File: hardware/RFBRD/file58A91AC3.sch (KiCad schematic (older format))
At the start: 19 parts

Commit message: Added bits of the RF Board, dumped to PCB.
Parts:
- added C34: 0.1uF, Capacitors_SMD:C_0805, symbol C
- added C35: 1uF, Capacitors_SMD:C_0805, symbol C
- added C36: 10uF, Capacitors_SMD:C_0805, symbol C
- added D1, D2: LED, LEDs:LED_0603, symbol LED
- added P1: CONN_01X08, Pin_Headers:Pin_Header_Straight_1x08, symbol CONN_01X08
- added R13: 1K, Resistors_SMD:R_0805, symbol R
- added W1, W2, W3, W4, W5, W6, W7, W8: TEST_1P, Measurement_Points:Test_Point_Keystone_5019_Minature, symbol TEST_1P
- 16MHz1: renamed from 16MHz; footprint (none) -> Crystals:Crystal_HC49-SD_SMD
- 9pF1, 9pF2: renamed from 9pF; footprint (none) -> Capacitors_SMD:C_0805
- C1, C2, C3, C4, C5, C6, C7, C8, C9: renamed from C?; footprint (none) -> Capacitors_SMD:C_0805
- L1: renamed from L?; footprint (none) -> Choke_SMD:Choke_SMD_7.3x7.3_H4.5
- L2, L3, L4, L5, L6: renamed from L?; footprint (none) -> Resistors_SMD:R_0805
- U1: renamed from U?; footprint (none) -> Housings_DFN_QFN:QFN-28-1EP_5x5mm_Pitch0.5mm
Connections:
- net labels added: VCC
- wire segments 76 -> 103
- no-connect marks 7 -> 8

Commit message: Added some Amplification Chain work.
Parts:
- removed W8: TEST_1P, Measurement_Points:Test_Point_Keystone_5019_Minature, symbol TEST_1P
- C37: renamed from 9pF1; value C -> 20pF
- C38: renamed from 9pF2; value C -> 20pF
- Y1: renamed from 16MHz1; value Crystal -> 16MHz
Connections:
- wire segments 103 -> 102
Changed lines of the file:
@@
 $EndComp
 $Comp
-L Crystal 16MHz1
+L Crystal Y1
 U 1 1 58A92FB4
 P 5550 2050
-F 0 "16MHz1" H 5550 2200 50  0000 C CNN
-F 1 "Crystal" H 5550 1900 50  0000 C CNN
+F 0 "Y1" H 5550 2200 50  0000 C CNN
+F 1 "16MHz" H 5550 1900 50  0000 C CNN
 F 2 "Crystals:Crystal_HC49-SD_SMD" H 5550 2050 50  0001 C CNN
 F 3 "" H 5550 2050 50  0000 C CNN
@@
 Connection ~ 5750 2050
 $Comp
-L C 9pF1
+L C C37
 U 1 1 58A93009
 P 5350 1700
-F 0 "9pF1" H 5375 1800 50  0000 L CNN
-F 1 "C" H 5375 1600 50  0000 L CNN
+F 0 "C37" H 5375 1800 50  0000 L CNN
+F 1 "20pF" H 5375 1600 50  0000 L CNN
 F 2 "Capacitors_SMD:C_0805" H 5388 1550 50  0001 C CNN
 F 3 "" H 5350 1700 50  0000 C CNN
@@
 $EndComp
 $Comp
-L C 9pF2
+L C C38
 U 1 1 58A93027
 P 5750 1700
-F 0 "9pF2" H 5775 1800 50  0000 L CNN
-F 1 "C" H 5775 1600 50  0000 L CNN
+F 0 "C38" H 5775 1800 50  0000 L CNN
+F 1 "20pF" H 5775 1600 50  0000 L CNN
 F 2 "Capacitors_SMD:C_0805" H 5788 1550 50  0001 C CNN
 F 3 "" H 5750 1700 50  0000 C CNN
@@
 Text GLabel 8700 1500 2    60   Input ~ 0
 uc_clk
-$Comp
-L TEST_1P W8
-U 1 1 58C35CC6
-P 9600 700
-F 0 "W8" H 9600 970 50  0000 C CNN
-F 1 "TEST_1P" H 9600 900 50  0000 C CNN
-F 2 "Measurement_Points:Test_Point_Keystone_5019_Minature" H 9800 700 50  0001 C CNN
-F 3 "" H 9800 700 50  0000 C CNN
-	1    9600 700
-	0    -1   -1   0
-$EndComp
-Wire Wire Line
-	9600 700  9700 700
-Text GLabel 9700 700  2    60   Input ~ 0
-PWRAMP_SEL
 $EndSCHEMATC

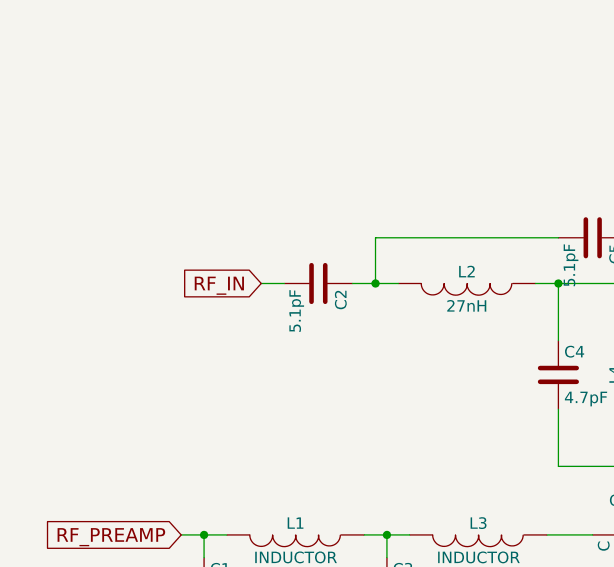
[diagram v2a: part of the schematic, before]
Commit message: Added Internals of Board.
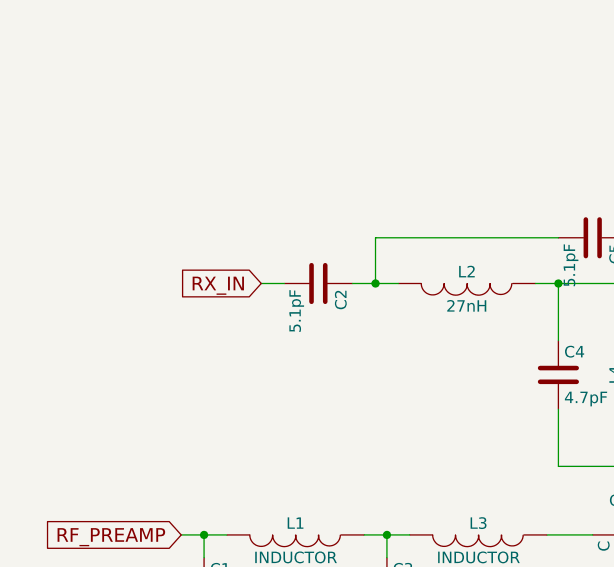
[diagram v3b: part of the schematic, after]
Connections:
- net labels added: RX_IN
- net labels removed: RF_IN
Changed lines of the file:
@@
 LIBS:contrib
 LIBS:valves
-LIBS:RFT
-LIBS:RFBRD-cache
 EELAYER 25 0
 EELAYER END
@@
 	2350 2750 2250 2750
 Text GLabel 2250 2750 0    60   Input ~ 0
-RF_IN
+RX_IN
 Wire Wire Line
 	6000 2450 6000 2250
